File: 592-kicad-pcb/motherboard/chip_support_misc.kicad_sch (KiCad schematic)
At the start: 8 parts, among them J6 2.54mm jumper, SW1 C318884, U6 74LVC1T45GW, U9 SN74LVC1G14DBV

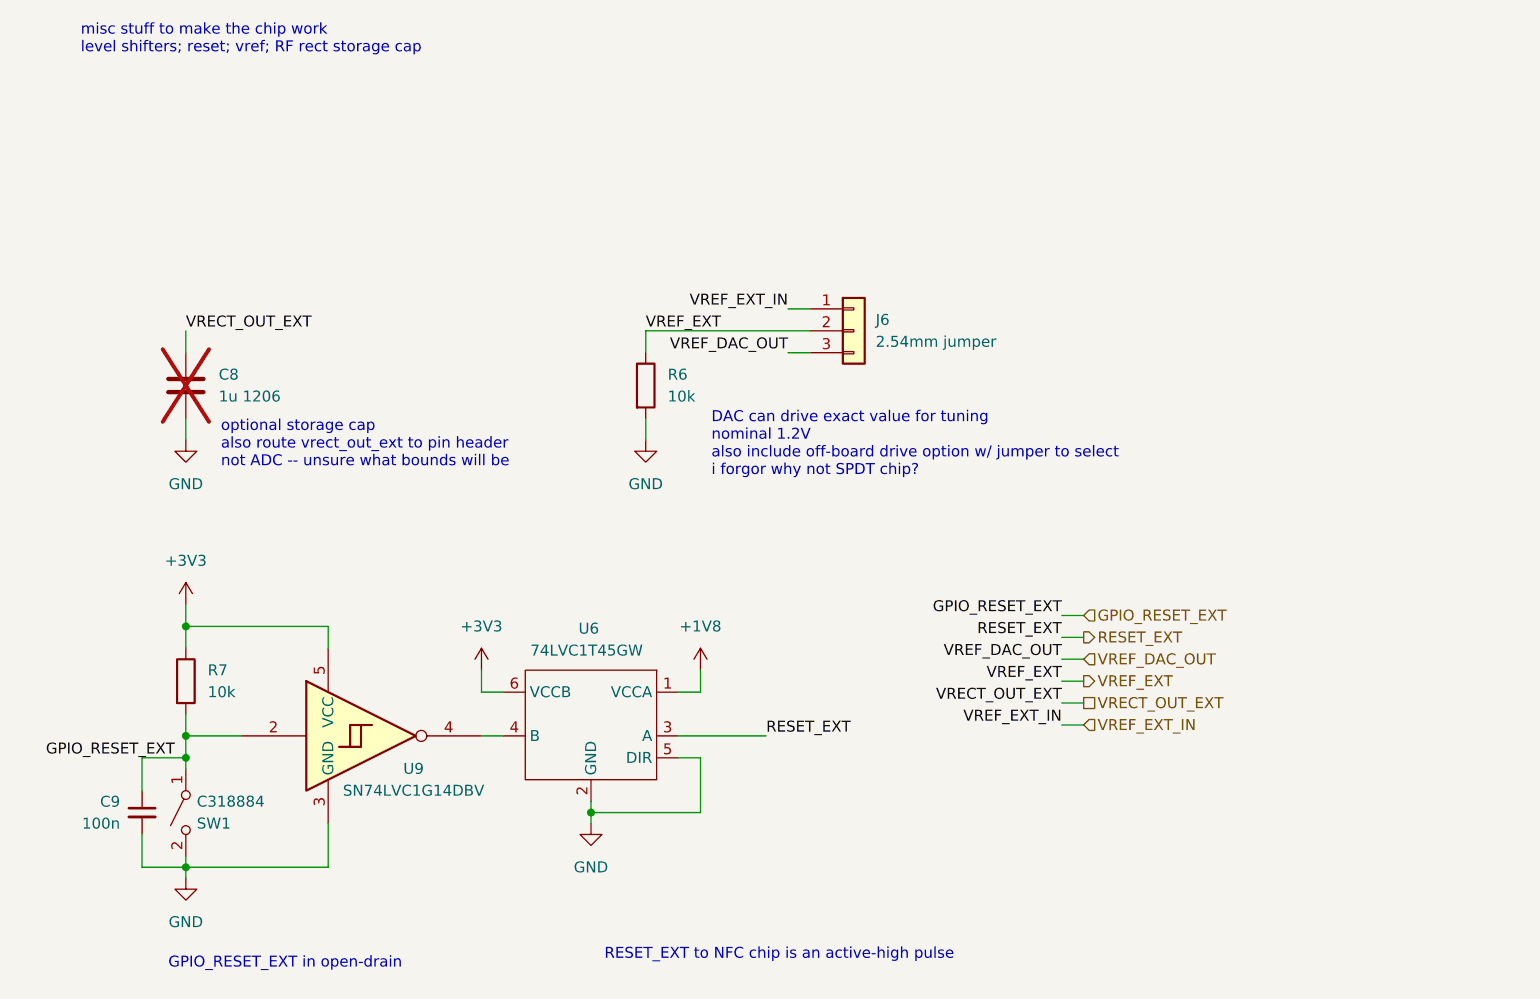
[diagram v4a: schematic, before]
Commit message: clean up schematics, add proper connectors
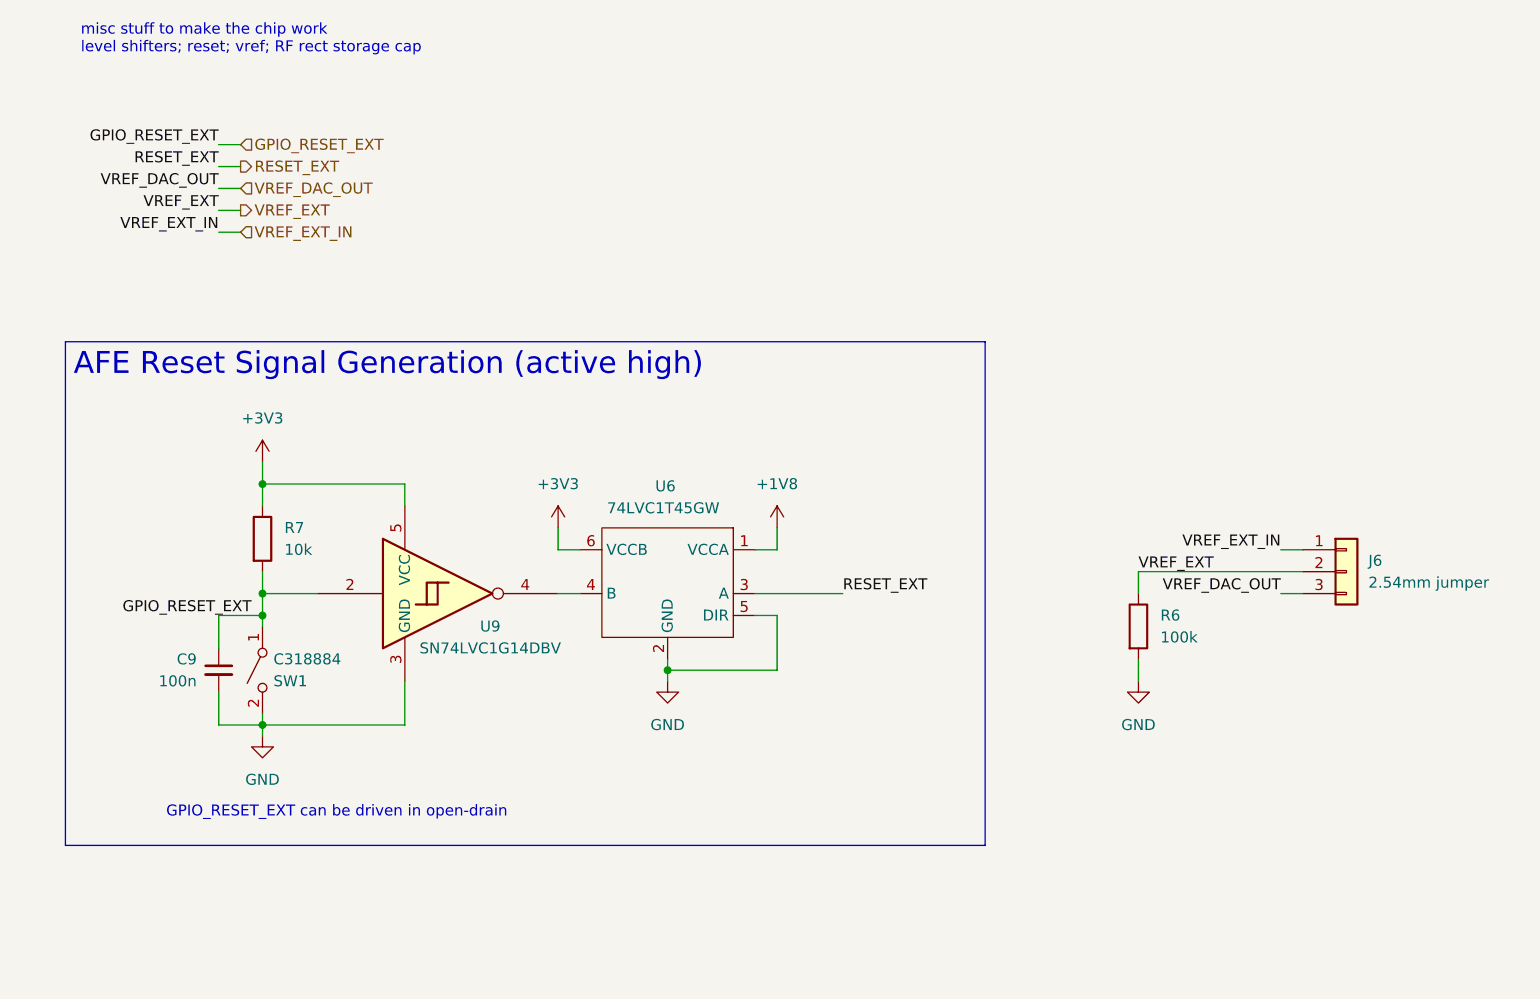
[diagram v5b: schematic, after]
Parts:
- removed C8: 1u 1206, Resistor_SMD:R_1206_3216Metric, symbol Device:C
- R6: value 10k -> 100k
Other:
- note added: "GPIO_RESET_EXT can be driven in open-drain"
- note removed: "DAC can drive exact value for tuning nominal 1.2V also include off-board drive option w/ jumper to select i forgor why not SPDT chip?"
- note removed: "GPIO_RESET_EXT in open-drain"
- note removed: "RESET_EXT to NFC chip is an active-high pulse"
- note removed: "optional storage cap also route vrect_out_ext to pin header not ADC -- unsure what bounds will be"
- moved on the sheet: C9, J6, R6, R7, SW1, U6, U9

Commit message: combine hierarchy of all sans power
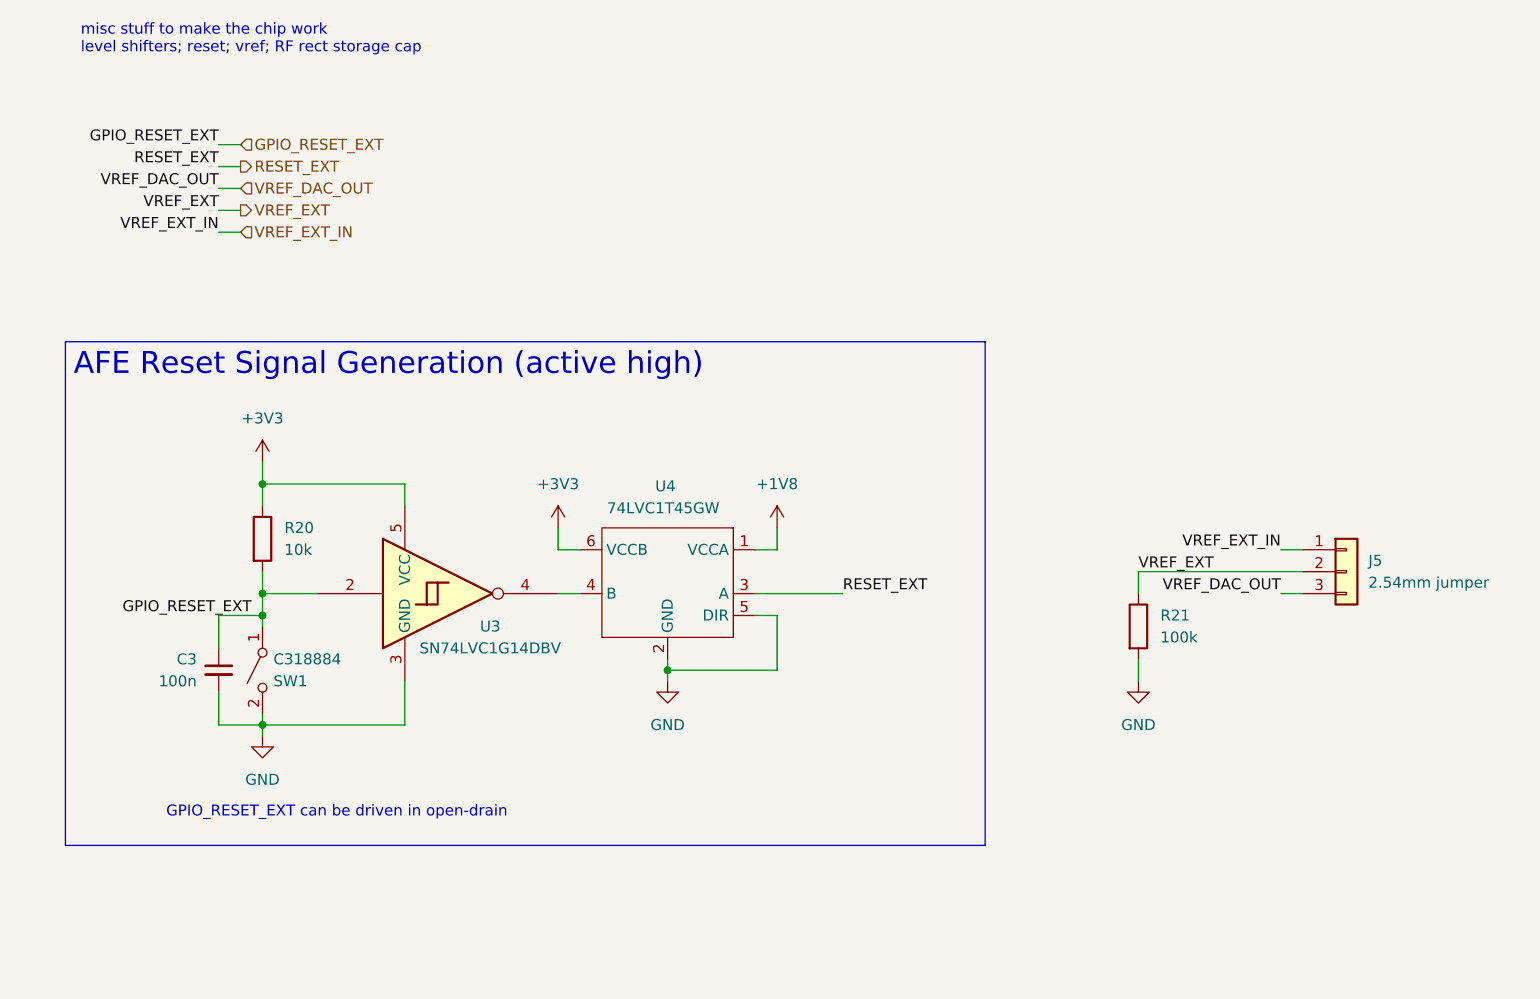
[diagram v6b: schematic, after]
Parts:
- renumbered C9 to C3, J6 to J5, R7 to R20, R6 to R21, U9 to U3, U6 to U4
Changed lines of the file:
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@@
 		(on_board yes)
 		(dnp no)
-		(property "Reference" "C9"
+		(property "Reference" "C3"
 			(at 35.56 92.7162 0)
 			(effects
@@
 		)
 		(instances
-			(project ""
-				(path "/5b0c97ac-fa03-4db8-b41b-0eee32b6f55d/1be5e80d-5a74-4ad9-b42f-508050f3350a"
-					(reference "C9")
+			(project "motherboard"
+				(path "/5b0c97ac-fa03-4db8-b41b-0eee32b6f55d/f049e4ad-bebe-4338-850a-2727de737ae9/43b528c2-ed3f-4c4d-855d-1f88d0a4fadb"
+					(reference "C3")
 					(unit 1)
 				)
@@
 		(on_board yes)
 		(dnp no)
-		(property "Reference" "U9"
+		(property "Reference" "U3"
 			(at 69.596 88.9 0)
 			(effects
@@
 		)
 		(instances
-			(project ""
-				(path "/5b0c97ac-fa03-4db8-b41b-0eee32b6f55d/1be5e80d-5a74-4ad9-b42f-508050f3350a"
-					(reference "U9")
+			(project "motherboard"
+				(path "/5b0c97ac-fa03-4db8-b41b-0eee32b6f55d/f049e4ad-bebe-4338-850a-2727de737ae9/43b528c2-ed3f-4c4d-855d-1f88d0a4fadb"
+					(reference "U3")
 					(unit 1)
 				)
@@
 		(dnp no)
 		(fields_autoplaced yes)
-		(property "Reference" "#PWR026"
+		(property "Reference" "#PWR057"
 			(at 90.17 101.6 0)
 			(effects
@@
 		(instances
 			(project "motherboard"
-				(path "/5b0c97ac-fa03-4db8-b41b-0eee32b6f55d/1be5e80d-5a74-4ad9-b42f-508050f3350a"
-					(reference "#PWR026")
+				(path "/5b0c97ac-fa03-4db8-b41b-0eee32b6f55d/f049e4ad-bebe-4338-850a-2727de737ae9/43b528c2-ed3f-4c4d-855d-1f88d0a4fadb"
+					(reference "#PWR057")
 					(unit 1)
 				)
@@
 		(dnp no)
 		(fields_autoplaced yes)
-		(property "Reference" "J6"
+		(property "Reference" "J5"
 			(at 171.45 81.2799 0)
 			(effects
@@
 		)
 		(instances
-			(project ""
-				(path "/5b0c97ac-fa03-4db8-b41b-0eee32b6f55d/1be5e80d-5a74-4ad9-b42f-508050f3350a"
-					(reference "J6")
+			(project "motherboard"
+				(path "/5b0c97ac-fa03-4db8-b41b-0eee32b6f55d/f049e4ad-bebe-4338-850a-2727de737ae9/43b528c2-ed3f-4c4d-855d-1f88d0a4fadb"
+					(reference "J5")
 					(unit 1)
 				)
@@
 		)
 		(instances
-			(project ""
-				(path "/5b0c97ac-fa03-4db8-b41b-0eee32b6f55d/1be5e80d-5a74-4ad9-b42f-508050f3350a"
+			(project "motherboard"
+				(path "/5b0c97ac-fa03-4db8-b41b-0eee32b6f55d/f049e4ad-bebe-4338-850a-2727de737ae9/43b528c2-ed3f-4c4d-855d-1f88d0a4fadb"
 					(reference "SW1")
 					(unit 1)
@@
 		(dnp no)
 		(fields_autoplaced yes)
-		(property "Reference" "#PWR028"
+		(property "Reference" "#PWR055"
 			(at 43.18 107.95 0)
 			(effects
@@
 		(instances
 			(project "motherboard"
-				(path "/5b0c97ac-fa03-4db8-b41b-0eee32b6f55d/1be5e80d-5a74-4ad9-b42f-508050f3350a"
-					(reference "#PWR028")
+				(path "/5b0c97ac-fa03-4db8-b41b-0eee32b6f55d/f049e4ad-bebe-4338-850a-2727de737ae9/43b528c2-ed3f-4c4d-855d-1f88d0a4fadb"
+					(reference "#PWR055")
 					(unit 1)
 				)
@@
 		(dnp no)
 		(fields_autoplaced yes)
-		(property "Reference" "#PWR024"
+		(property "Reference" "#PWR059"
 			(at 144.78 101.6 0)
 			(effects
@@
 		(instances
 			(project "motherboard"
-				(path "/5b0c97ac-fa03-4db8-b41b-0eee32b6f55d/1be5e80d-5a74-4ad9-b42f-508050f3350a"
-					(reference "#PWR024")
+				(path "/5b0c97ac-fa03-4db8-b41b-0eee32b6f55d/f049e4ad-bebe-4338-850a-2727de737ae9/43b528c2-ed3f-4c4d-855d-1f88d0a4fadb"
+					(reference "#PWR059")
 					(unit 1)
 				)
@@
 		(on_board yes)
 		(dnp no)
-		(property "Reference" "#PWR025"
+		(property "Reference" "#PWR058"
 			(at 102.87 81.28 0)
 			(effects
@@
 		(instances
 			(project "motherboard"
-				(path "/5b0c97ac-fa03-4db8-b41b-0eee32b6f55d/1be5e80d-5a74-4ad9-b42f-508050f3350a"
-					(reference "#PWR025")
+				(path "/5b0c97ac-fa03-4db8-b41b-0eee32b6f55d/f049e4ad-bebe-4338-850a-2727de737ae9/43b528c2-ed3f-4c4d-855d-1f88d0a4fadb"
+					(reference "#PWR058")
 					(unit 1)
 				)
@@
 		(dnp no)
 		(fields_autoplaced yes)
-		(property "Reference" "R7"
+		(property "Reference" "R20"
 			(at 45.72 77.4699 0)
 			(effects
@@
 		(instances
 			(project "motherboard"
-				(path "/5b0c97ac-fa03-4db8-b41b-0eee32b6f55d/1be5e80d-5a74-4ad9-b42f-508050f3350a"
-					(reference "R7")
+				(path "/5b0c97ac-fa03-4db8-b41b-0eee32b6f55d/f049e4ad-bebe-4338-850a-2727de737ae9/43b528c2-ed3f-4c4d-855d-1f88d0a4fadb"
+					(reference "R20")
 					(unit 1)
 				)
@@
 		(on_board yes)
 		(dnp no)
-		(property "Reference" "U6"
+		(property "Reference" "U4"
 			(at 89.916 72.644 0)
 			(effects
@@
 		(instances
 			(project "motherboard"
-				(path "/5b0c97ac-fa03-4db8-b41b-0eee32b6f55d/1be5e80d-5a74-4ad9-b42f-508050f3350a"
-					(reference "U6")
+				(path "/5b0c97ac-fa03-4db8-b41b-0eee32b6f55d/f049e4ad-bebe-4338-850a-2727de737ae9/43b528c2-ed3f-4c4d-855d-1f88d0a4fadb"
+					(reference "U4")
 					(unit 1)
 				)
@@
 		(on_board yes)
 		(dnp no)
-		(property "Reference" "#PWR027"
+		(property "Reference" "#PWR056"
 			(at 77.47 81.28 0)
 			(effects
@@
 		(instances
 			(project "motherboard"
-				(path "/5b0c97ac-fa03-4db8-b41b-0eee32b6f55d/1be5e80d-5a74-4ad9-b42f-508050f3350a"
-					(reference "#PWR027")
+				(path "/5b0c97ac-fa03-4db8-b41b-0eee32b6f55d/f049e4ad-bebe-4338-850a-2727de737ae9/43b528c2-ed3f-4c4d-855d-1f88d0a4fadb"
+					(reference "#PWR056")
 					(unit 1)
 				)
@@
 		(dnp no)
 		(fields_autoplaced yes)
-		(property "Reference" "R6"
+		(property "Reference" "R21"
 			(at 147.32 87.6299 0)
 			(effects
@@
 		)
 		(instances
-			(project ""
-				(path "/5b0c97ac-fa03-4db8-b41b-0eee32b6f55d/1be5e80d-5a74-4ad9-b42f-508050f3350a"
-					(reference "R6")
+			(project "motherboard"
+				(path "/5b0c97ac-fa03-4db8-b41b-0eee32b6f55d/f049e4ad-bebe-4338-850a-2727de737ae9/43b528c2-ed3f-4c4d-855d-1f88d0a4fadb"
+					(reference "R21")
 					(unit 1)
 				)
@@
 		(on_board yes)
 		(dnp no)
-		(property "Reference" "#PWR029"
+		(property "Reference" "#PWR054"
 			(at 43.18 73.66 0)
 			(effects
@@
 		(instances
 			(project "motherboard"
-				(path "/5b0c97ac-fa03-4db8-b41b-0eee32b6f55d/1be5e80d-5a74-4ad9-b42f-508050f3350a"
-					(reference "#PWR029")
-					(unit 1)
-				)
+				(path "/5b0c97ac-fa03-4db8-b41b-0eee32b6f55d/f049e4ad-bebe-4338-850a-2727de737ae9/43b528c2-ed3f-4c4d-855d-1f88d0a4fadb"
+					(reference "#PWR054")
+					(unit 1)
+				)

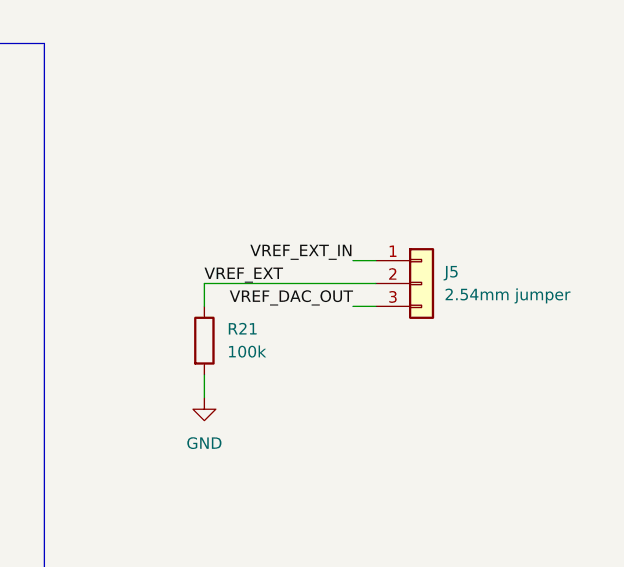
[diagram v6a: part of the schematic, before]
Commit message: add JLC part num for parts, footprints
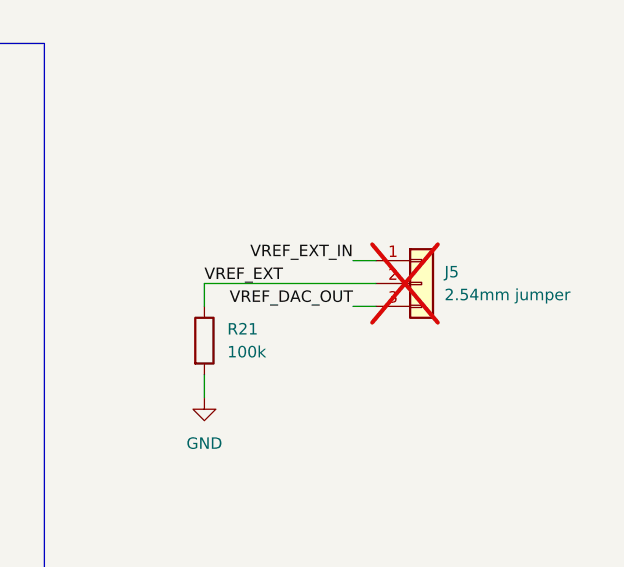
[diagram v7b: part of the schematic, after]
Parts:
- C3: footprint Capacitor_SMD:C_0603_1608Metric -> Capacitor_SMD:C_0402_1005Metric; LCSC (none) -> C1525
- J5: now not fitted
- R20: footprint Resistor_SMD:R_0603_1608Metric -> Resistor_SMD:R_0402_1005Metric; LCSC (none) -> C25744
- R21: footprint Resistor_SMD:R_0603_1608Metric -> Resistor_SMD:R_0402_1005Metric; LCSC (none) -> C25741
- SW1: LCSC (none) -> C318884
- U3: footprint Package_TO_SOT_SMD:SOT-23-5 -> Package_TO_SOT_SMD:SOT-353_SC-70-5; LCSC (none) -> C35740
- U4: LCSC (none) -> C478004
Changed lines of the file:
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@@
 			)
 		)
-		(property "Footprint" "Capacitor_SMD:C_0603_1608Metric"
+		(property "Footprint" "Capacitor_SMD:C_0402_1005Metric"
 			(at 38.1 93.98 0)
 			(effects
@@
 			)
 		)
+		(property "LCSC" "C1525"
+			(at 38.1 93.98 0)
+			(effects
+				(font
+					(size 1.27 1.27)
+				)
+				(hide yes)
+			)
+		)
 		(pin "1"
 		)
@@
 			)
 		)
-		(property "Footprint" "Package_TO_SOT_SMD:SOT-23-5"
+		(property "Footprint" "Package_TO_SOT_SMD:SOT-353_SC-70-5"
 			(at 64.77 91.44 0)
 			(effects
@@
 		)
 		(property "Description" "Single Schmitt NOT Gate, Low-Voltage CMOS, SOT-23"
+			(at 64.77 85.09 0)
+			(effects
+				(font
+					(size 1.27 1.27)
+				)
+				(hide yes)
+			)
+		)
+		(property "LCSC" "C35740"
 			(at 64.77 85.09 0)
 			(effects
@@
 		(in_bom yes)
 		(on_board yes)
-		(dnp no)
+		(dnp yes)
 		(fields_autoplaced yes)
 		(property "Reference" "J5"
@@
 			)
 		)
+		(property "LCSC" "C318884"
+			(at 43.18 93.98 90)
+			(effects
+				(font
+					(size 1.27 1.27)
+				)
+				(hide yes)
+			)
+		)
 		(pin "1"
 		)
@@
 			)
 		)
-		(property "Footprint" "Resistor_SMD:R_0603_1608Metric"
+		(property "Footprint" "Resistor_SMD:R_0402_1005Metric"
 			(at 41.402 78.74 90)
 			(effects
@@
 		)
 		(property "Description" "Resistor"
+			(at 43.18 78.74 0)
+			(effects
+				(font
+					(size 1.27 1.27)
+				)
+				(hide yes)
+			)
+		)
+		(property "LCSC" "C25744"
 			(at 43.18 78.74 0)
 			(effects
@@
 			)
 		)
+		(property "LCSC" "C478004"
+			(at 90.17 83.82 0)
+			(effects
+				(font
+					(size 1.27 1.27)
+				)
+				(hide yes)
+			)
+		)
 		(pin "4"
 		)
@@
 			)
 		)
-		(property "Footprint" "Resistor_SMD:R_0603_1608Metric"
+		(property "Footprint" "Resistor_SMD:R_0402_1005Metric"
 			(at 143.002 88.9 90)
 			(effects
@@
 			(at 144.78 88.9 0)
 			(effects
+				(font
+					(size 1.27 1.27)
+				)
+				(hide yes)
+			)
+		)
+		(property "LCSC" "C25741"
+			(at 144.78 88.9 0)
+			(effects
